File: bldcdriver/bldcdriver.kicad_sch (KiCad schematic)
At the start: 1 part, among them U1 DRV8304HRHAR

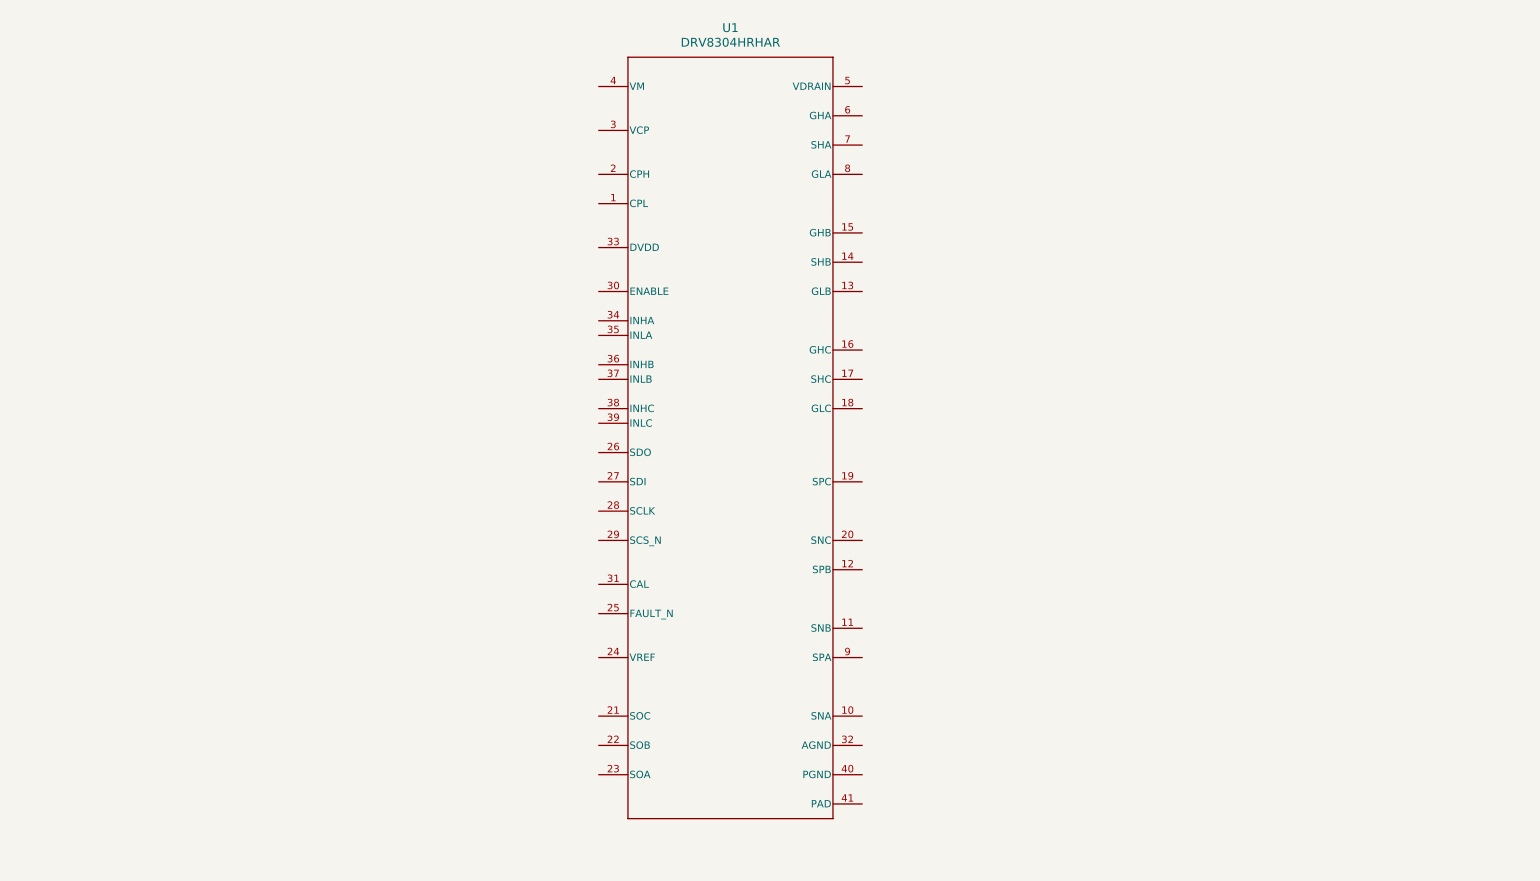
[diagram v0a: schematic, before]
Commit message: Finished N MOSFET Triple Half Bridge Circuit with Global Labels, looking if I want to use a P MOSFET
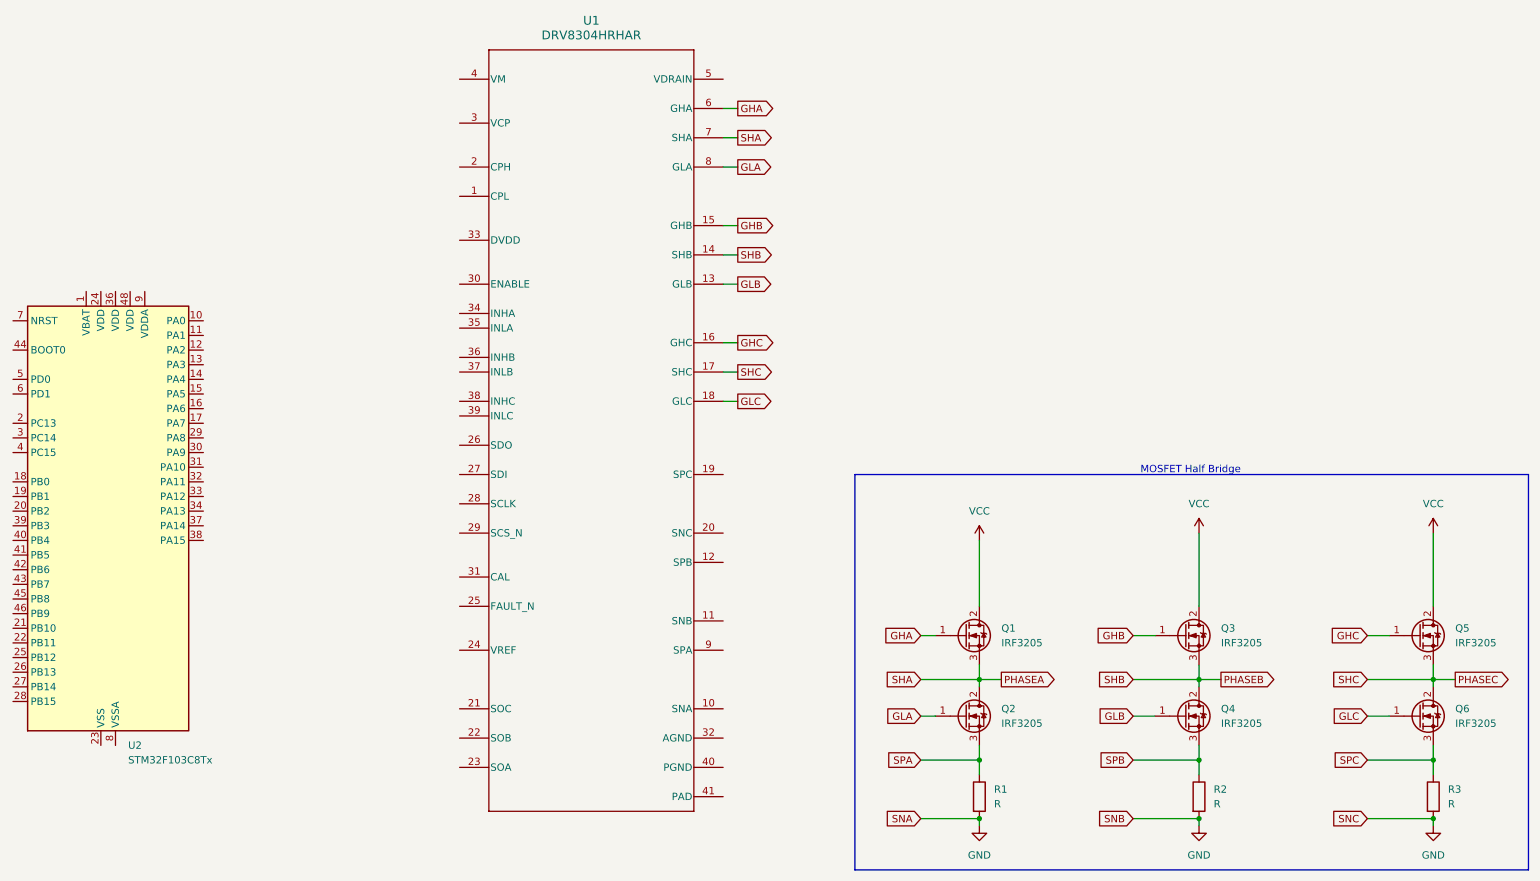
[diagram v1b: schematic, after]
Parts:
- added Q1, Q2, Q3, Q4, Q5, Q6: IRF3205, Package_TO_SOT_THT:TO-220-3_Horizontal_TabDown, symbol Transistor_FET:IRF3205
- added R1, R2, R3: R, symbol Device:R
- added U2: STM32F103C8Tx, Package_QFP:LQFP-48_7x7mm_P0.5mm, symbol MCU_ST_STM32F1:STM32F103C8Tx
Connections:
- net GLB: now reaches U1.13 (GLB)
- net GLB: now also Q4.1 (G)
- net PHASEB: now reaches U1.14 (SHB)
- net PHASEB: now also Q3.3 (S), Q4.2 (D)
- net GHB: now reaches U1.15 (GHB)
- net GHB: now also Q3.1 (G)
- net GHC: now reaches U1.16 (GHC)
- net GHC: now also Q5.1 (G)
- net PHASEC: now reaches U1.17 (SHC)
- net PHASEC: now also Q5.3 (S), Q6.2 (D)
- net GLC: now reaches U1.18 (GLC)
- net GLC: now also Q6.1 (G)
- net GHA: now reaches U1.6 (GHA)
- net GHA: now also Q1.1 (G)
- net PHASEA: now reaches U1.7 (SHA)
- net PHASEA: now also Q1.3 (S), Q2.2 (D)
- net GLA: now reaches U1.8 (GLA)
- net GLA: now also Q2.1 (G)
- new net: U2.23 (VSS), U2.35 (VSS), U2.47 (VSS)
- new net GND: R1.2, R2.2, R3.2
- new net SPA: Q2.3 (S), R1.1
- new net SPB: Q4.3 (S), R2.1
- new net SPC: Q6.3 (S), R3.1
- new net VCC: Q1.2 (D), Q3.2 (D), Q5.2 (D)
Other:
- note added: "MOSFET Half Bridge"
- moved on the sheet: U1

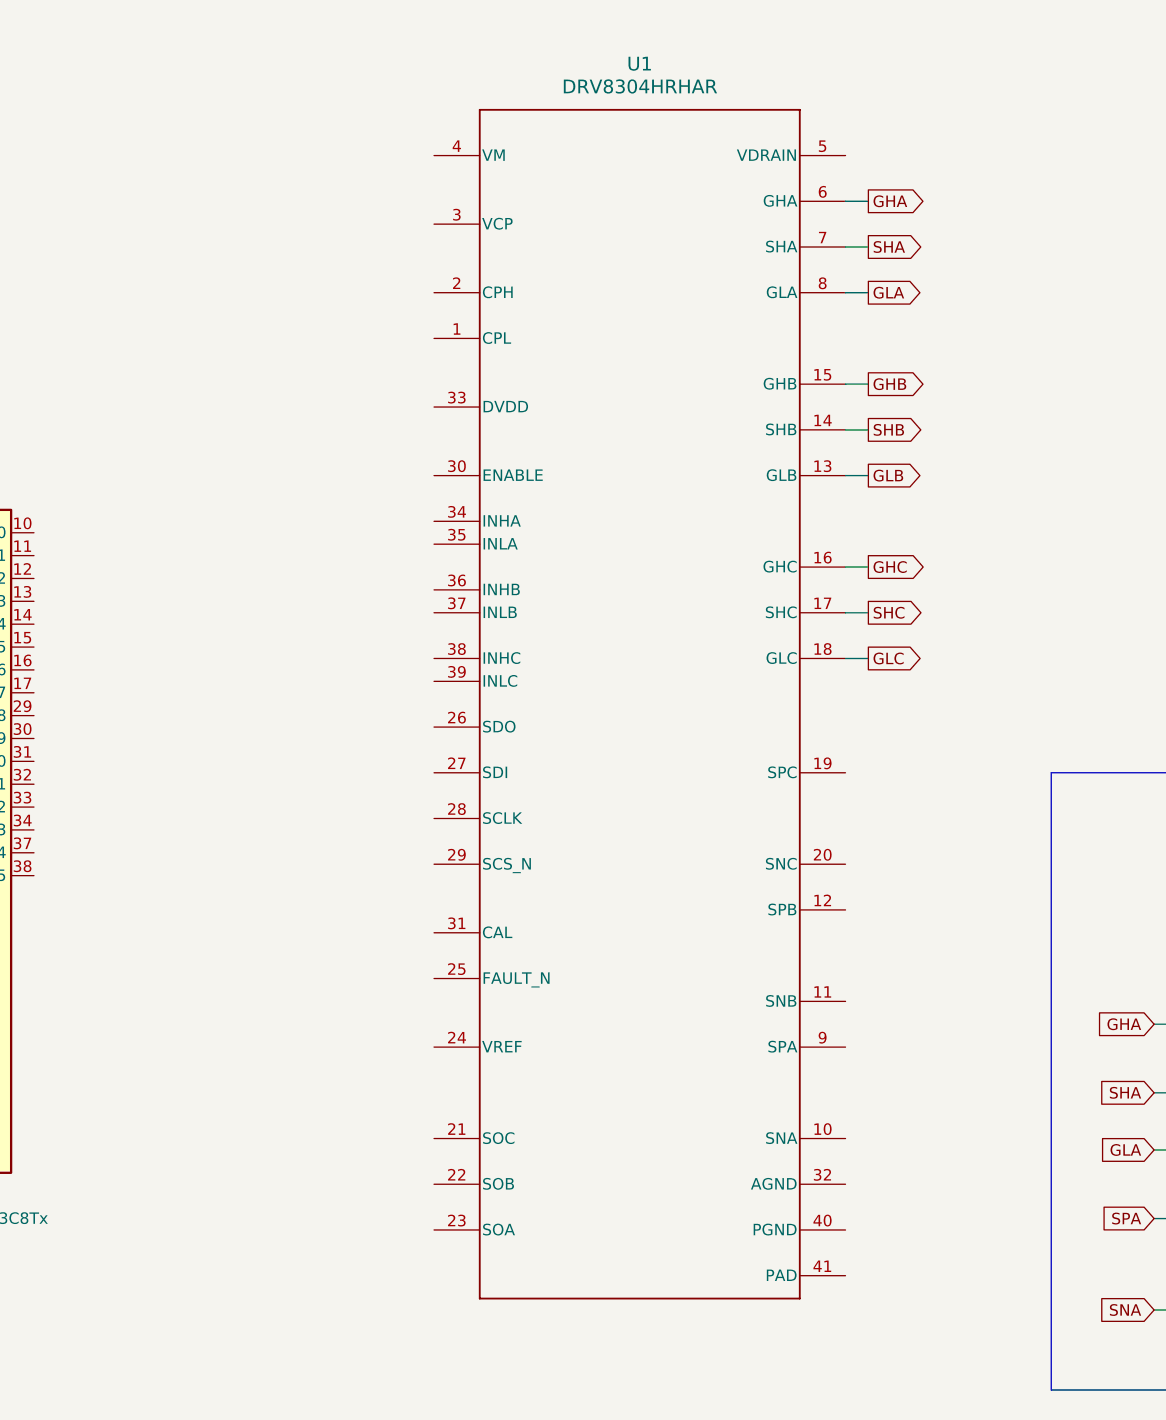
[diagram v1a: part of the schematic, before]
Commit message: Few more connections and capacitors
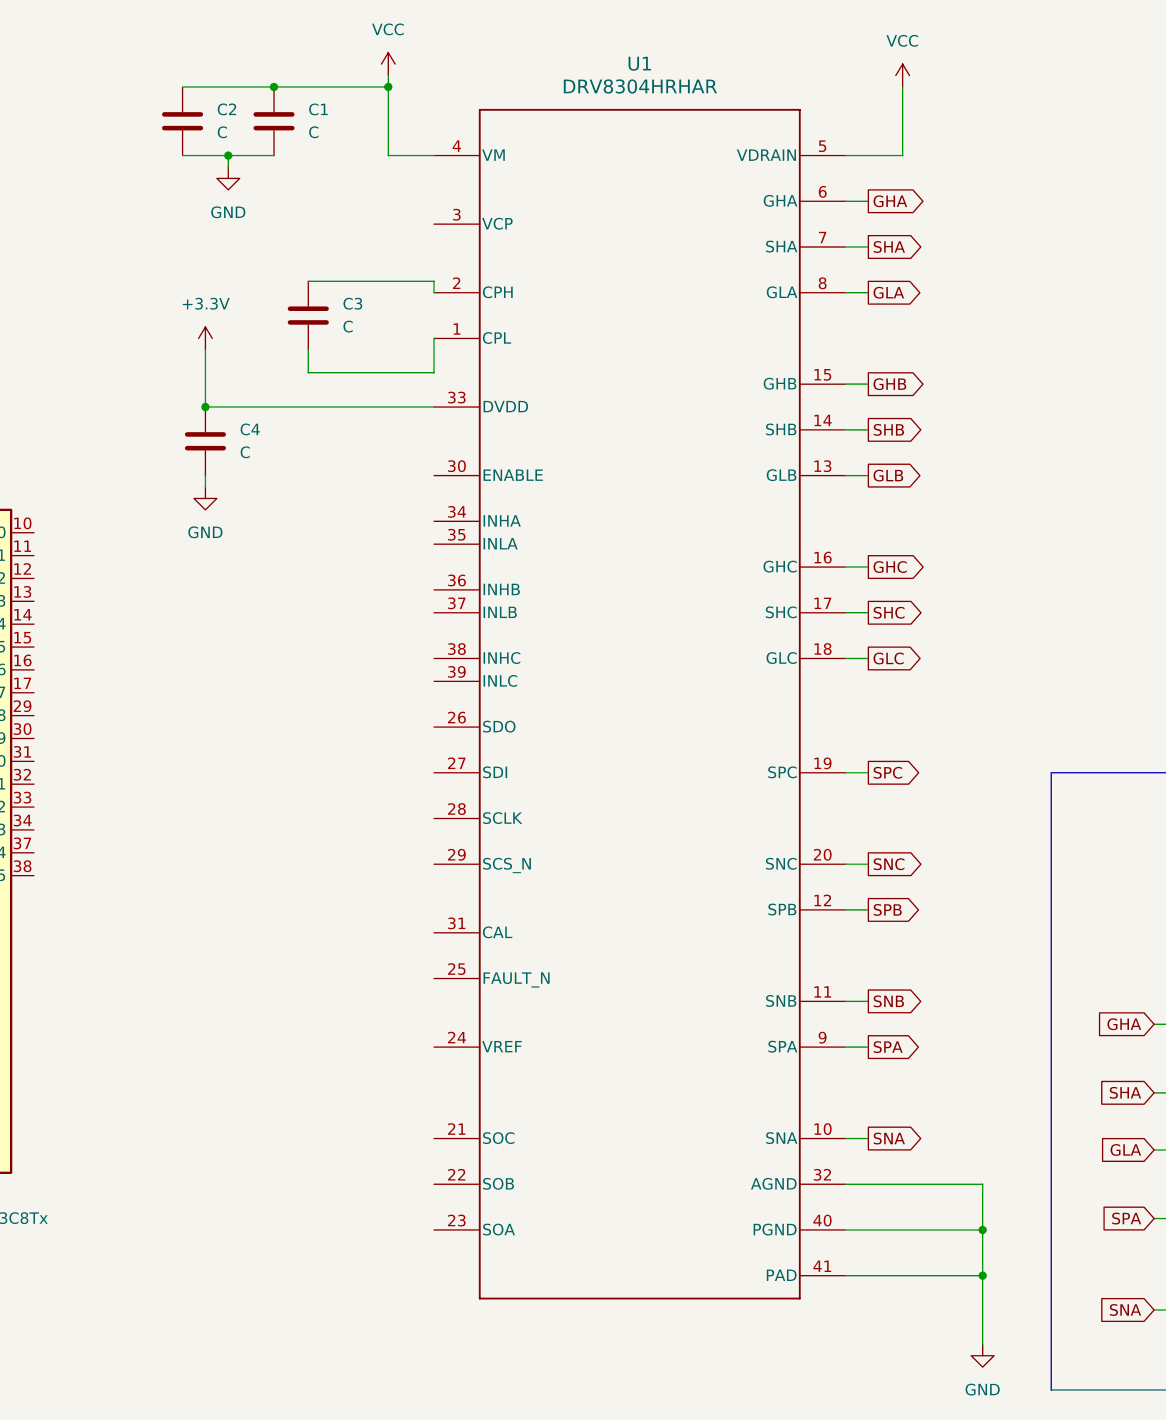
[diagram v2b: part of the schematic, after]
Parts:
- added C1, C2, C3, C4: C, symbol Device:C
- R1, R2, R3: footprint (none) -> Resistor_SMD:R_0201_0603Metric
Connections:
- net GND: now also U1.10 (SNA), U1.11 (SNB), U1.20 (SNC), U1.32 (AGND), U1.40 (PGND), U1.41 (PAD), C1.2, C2.2, C4.2
- net SPA: now also U1.9 (SPA)
- net SPB: now also U1.12 (SPB)
- net SPC: now also U1.19 (SPC)
- net VCC: now also U1.4 (VM), U1.5 (VDRAIN), C1.1, C2.1
- net at U1.1 (CPL): now also C3.2
- net at U1.2 (CPH): now also C3.1
- net +3.3V: now reaches U1.33 (DVDD)
- net +3.3V: now also C4.1

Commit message: Few changes, not sure
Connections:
- net GND: now also U2.23 (VSS), U2.35 (VSS), U2.47 (VSS), U2.8 (VSSA)
- net VCC: now also U2.1 (VBAT), U2.24 (VDD), U2.36 (VDD), U2.48 (VDD), U2.9 (VDDA)
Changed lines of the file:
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@@
   (junction (at 187.96 146.05) (diameter 0) (color 0 0 0 0)
   )
+  (junction (at 40.64 62.23) (diameter 0) (color 0 0 0 0)
+  )
   (junction (at 92.71 20.32) (diameter 0) (color 0 0 0 0)
   )
   (junction (at 158.75 147.32) (diameter 0) (color 0 0 0 0)
   )
+  (junction (at 35.56 62.23) (diameter 0) (color 0 0 0 0)
+  )
   (junction (at 158.75 152.4) (diameter 0) (color 0 0 0 0)
   )
+  (junction (at 38.1 62.23) (diameter 0) (color 0 0 0 0)
+  )
   (junction (at 226.06 146.05) (diameter 0) (color 0 0 0 0)
   )
@@
   (junction (at 266.7 156.21) (diameter 0) (color 0 0 0 0)
   )
+  (junction (at 36.83 144.78) (diameter 0) (color 0 0 0 0)
+  )
   (junction (at 266.7 146.05) (diameter 0) (color 0 0 0 0)
   )
@@
     (stroke (width 0) (type default))
   )
+  (wire (pts (xy 35.56 143.51) (xy 35.56 144.78))
+    (stroke (width 0) (type default))
+  )
   (wire (pts (xy 143.51 33.02) (xy 146.05 33.02))
     (stroke (width 0) (type default))
   )
+  (wire (pts (xy 38.1 62.23) (xy 38.1 64.77))
+    (stroke (width 0) (type default))
+  )
   (wire (pts (xy 80.01 20.32) (xy 92.71 20.32))
     (stroke (width 0) (type default))
@@
     (stroke (width 0) (type default))
   )
+  (wire (pts (xy 36.83 144.78) (xy 38.1 144.78))
+    (stroke (width 0) (type default))
+  )
+  (wire (pts (xy 35.56 64.77) (xy 35.56 62.23))
+    (stroke (width 0) (type default))
+  )
   (wire (pts (xy 266.7 106.68) (xy 266.7 119.38))
     (stroke (width 0) (type default))
@@
     (stroke (width 0) (type default))
   )
+  (wire (pts (xy 38.1 58.42) (xy 38.1 62.23))
+    (stroke (width 0) (type default))
+  )
+  (wire (pts (xy 38.1 62.23) (xy 40.64 62.23))
+    (stroke (width 0) (type default))
+  )
   (wire (pts (xy 143.51 127) (xy 146.05 127))
     (stroke (width 0) (type default))
@@
     (stroke (width 0) (type default))
   )
+  (wire (pts (xy 38.1 143.51) (xy 38.1 144.78))
+    (stroke (width 0) (type default))
+  )
+  (wire (pts (xy 35.56 62.23) (xy 33.02 62.23))
+    (stroke (width 0) (type default))
+  )
   (wire (pts (xy 158.75 142.24) (xy 158.75 147.32))
     (stroke (width 0) (type default))
@@
     (stroke (width 0) (type default))
   )
+  (wire (pts (xy 40.64 62.23) (xy 43.18 62.23))
+    (stroke (width 0) (type default))
+  )
   (wire (pts (xy 143.51 27.94) (xy 149.86 27.94))
     (stroke (width 0) (type default))
@@
     (stroke (width 0) (type default))
   )
+  (wire (pts (xy 33.02 62.23) (xy 33.02 64.77))
+    (stroke (width 0) (type default))
+  )
+  (wire (pts (xy 40.64 62.23) (xy 40.64 64.77))
+    (stroke (width 0) (type default))
+  )
   (wire (pts (xy 226.06 132.08) (xy 226.06 133.35))
     (stroke (width 0) (type default))
@@
     (stroke (width 0) (type default))
   )
+  (wire (pts (xy 43.18 62.23) (xy 43.18 64.77))
+    (stroke (width 0) (type default))
+  )
   (wire (pts (xy 74.93 27.94) (xy 74.93 29.21))
     (stroke (width 0) (type default))
@@
     (stroke (width 0) (type default))
   )
+  (wire (pts (xy 35.56 62.23) (xy 38.1 62.23))
+    (stroke (width 0) (type default))
+  )
   (wire (pts (xy 226.06 143.51) (xy 226.06 146.05))
     (stroke (width 0) (type default))
@@
   )
   (wire (pts (xy 266.7 156.21) (xy 266.7 157.48))
+    (stroke (width 0) (type default))
+  )
+  (wire (pts (xy 35.56 144.78) (xy 36.83 144.78))
     (stroke (width 0) (type default))
   )
@@
     (property "Intersheetrefs" "${INTERSHEET_REFS}" (at 208.0767 138.43 0)
       (effects (font (size 1.27 1.27)) (justify right) hide)
+    )
+  )
+  (symbol (lib_id "power:VCC") (at 38.1 58.42 0) (unit 1)
+    (in_bom yes) (on_board yes) (dnp no) (fields_autoplaced)
+    (property "Reference" "#PWR013" (at 38.1 62.23 0)
+      (effects (font (size 1.27 1.27)) hide)
+    )
+    (property "Value" "VCC" (at 38.1 53.34 0)
+      (effects (font (size 1.27 1.27)))
+    )
+    (property "Footprint" "" (at 38.1 58.42 0)
+      (effects (font (size 1.27 1.27)) hide)
+    )
+    (property "Datasheet" "" (at 38.1 58.42 0)
+      (effects (font (size 1.27 1.27)) hide)
+    )
+    (pin "1")
+    (instances
+      (project "bldcdriver"
+        (path "/386247e7-fbba-4db7-978d-7d877f3805e6"
+          (reference "#PWR013") (unit 1)
+        )
+      )
     )
   )
@@
         )
       )
+    )
+  )
+  (symbol (lib_id "power:GND") (at 36.83 144.78 0) (unit 1)
+    (in_bom yes) (on_board yes) (dnp no) (fields_autoplaced)
+    (property "Reference" "#PWR014" (at 36.83 151.13 0)
+      (effects (font (size 1.27 1.27)) hide)
+    )
+    (property "Value" "GND" (at 36.83 149.86 0)
+      (effects (font (size 1.27 1.27)))
+    )
+    (property "Footprint" "" (at 36.83 144.78 0)
+      (effects (font (size 1.27 1.27)) hide)
+    )
+    (property "Datasheet" "" (at 36.83 144.78 0)
+      (effects (font (size 1.27 1.27)) hide)
+    )
+    (pin "1")
+    (instances
+      (project "bldcdriver"
+        (path "/386247e7-fbba-4db7-978d-7d877f3805e6"
+          (reference "#PWR014") (unit 1)
+        )
+      )

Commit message: Replaced STM32 with RP2040
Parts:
- removed U2: STM32F103C8Tx, Package_QFP:LQFP-48_7x7mm_P0.5mm, symbol MCU_ST_STM32F1:STM32F103C8Tx
- added C5: 1uF, symbol Device:C
- added U2: RP2040, Package_DFN_QFN:QFN-56-1EP_7x7mm_P0.4mm_EP3.2x3.2mm, symbol MCU_RaspberryPi:RP2040
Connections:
- net +3.3V: now also U1.24 (VREF)
- net GND: now also U1.31 (CAL), U2.57 (GND)
- net at U1.3 (VCP): now also C5.2
- net VCC renamed +24V
- net +24V: now also C5.1
- new net: U2.1 (IOVDD), U2.10 (IOVDD), U2.22 (IOVDD), U2.33 (IOVDD), U2.42 (IOVDD), U2.49 (IOVDD)
- new net: U2.23 (DVDD), U2.50 (DVDD)
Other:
- added sheet Power Sheet (power_bldc.kicad_sch)
- added sheet Three Phase Half Bridge (3halfbridge.kicad_sch)
- note added: "X5R/X7R 16V Capacitor"
- moved on the sheet: C1, C2, C3, C4, U1
